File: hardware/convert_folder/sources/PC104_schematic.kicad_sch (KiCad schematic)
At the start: 33 parts, among them CN20 PC104_inverted, CN21 PC104, CN22 PC104, CN23 PC104, CN24 PC104, CN25 PC104

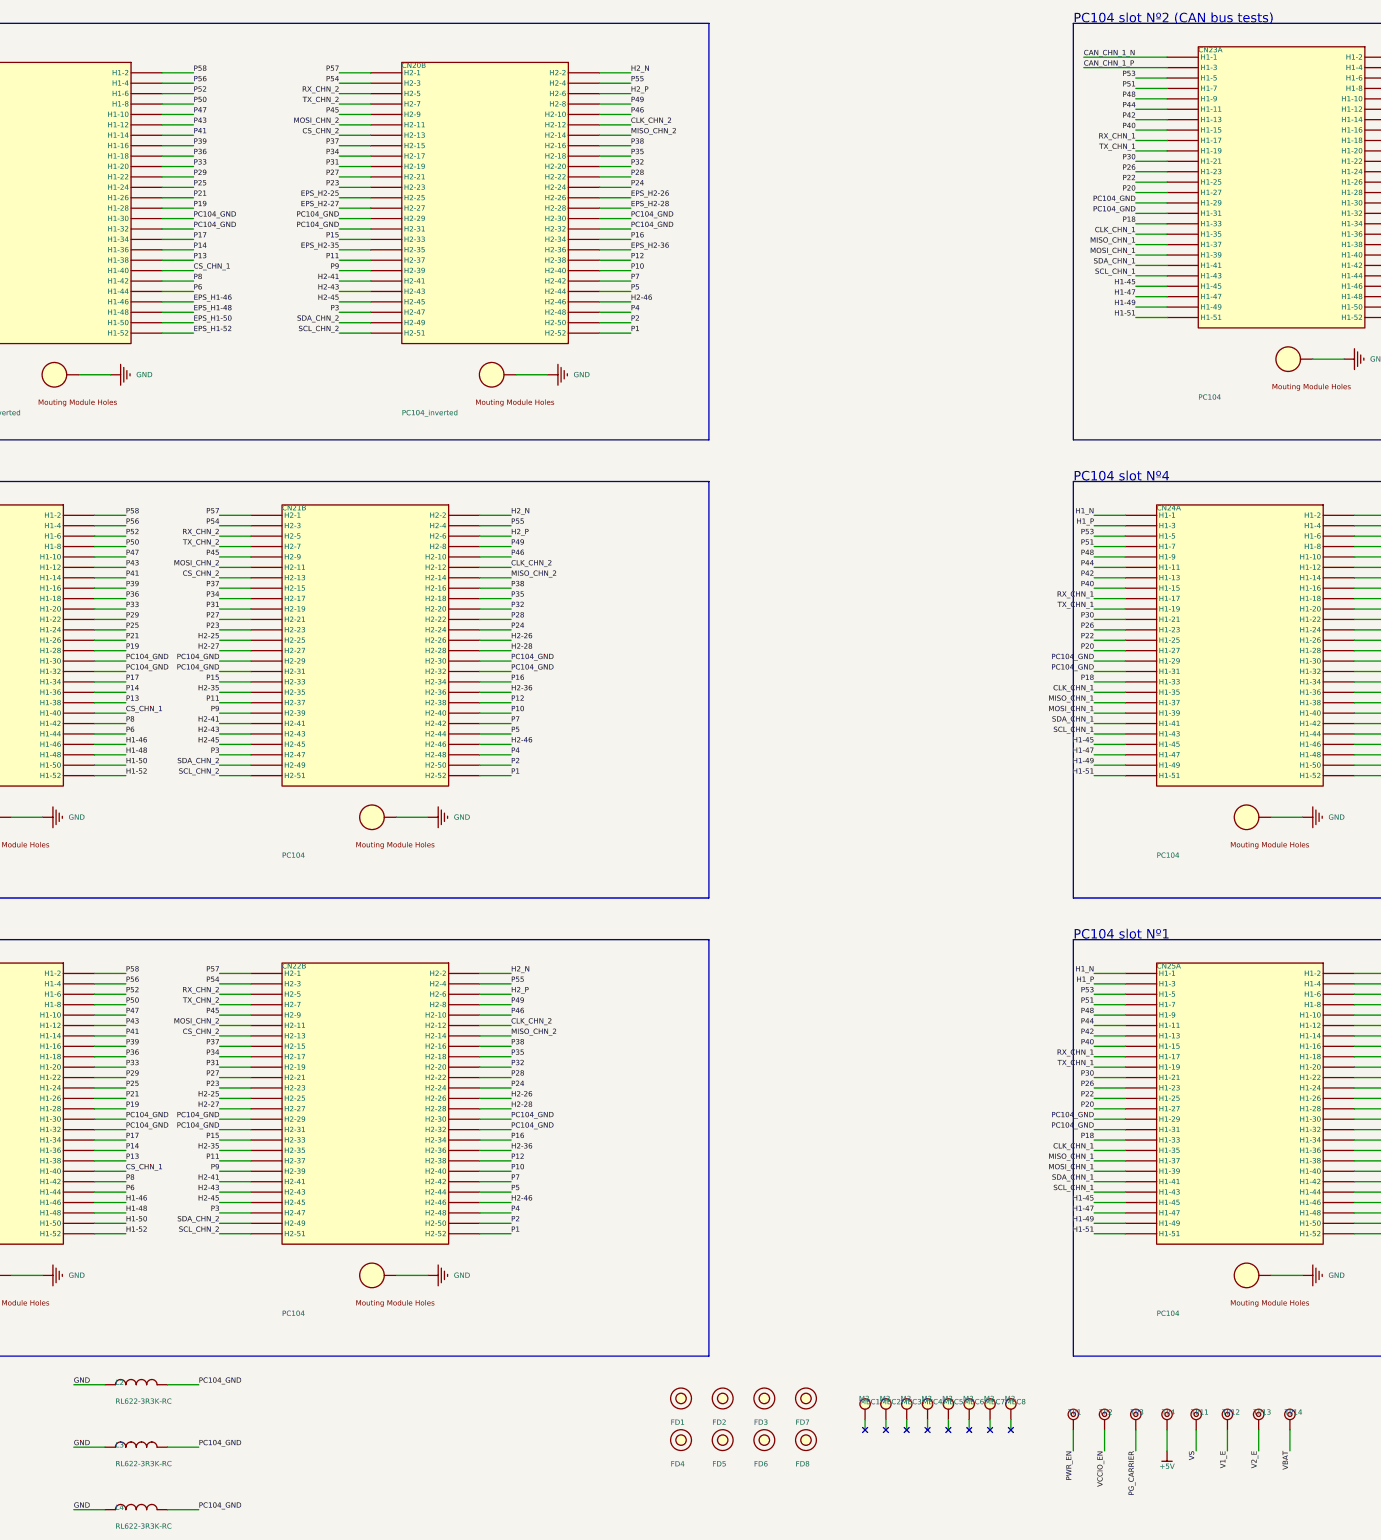
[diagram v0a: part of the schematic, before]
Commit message: fix: fix a lot of connections between blocks. Many more to go...
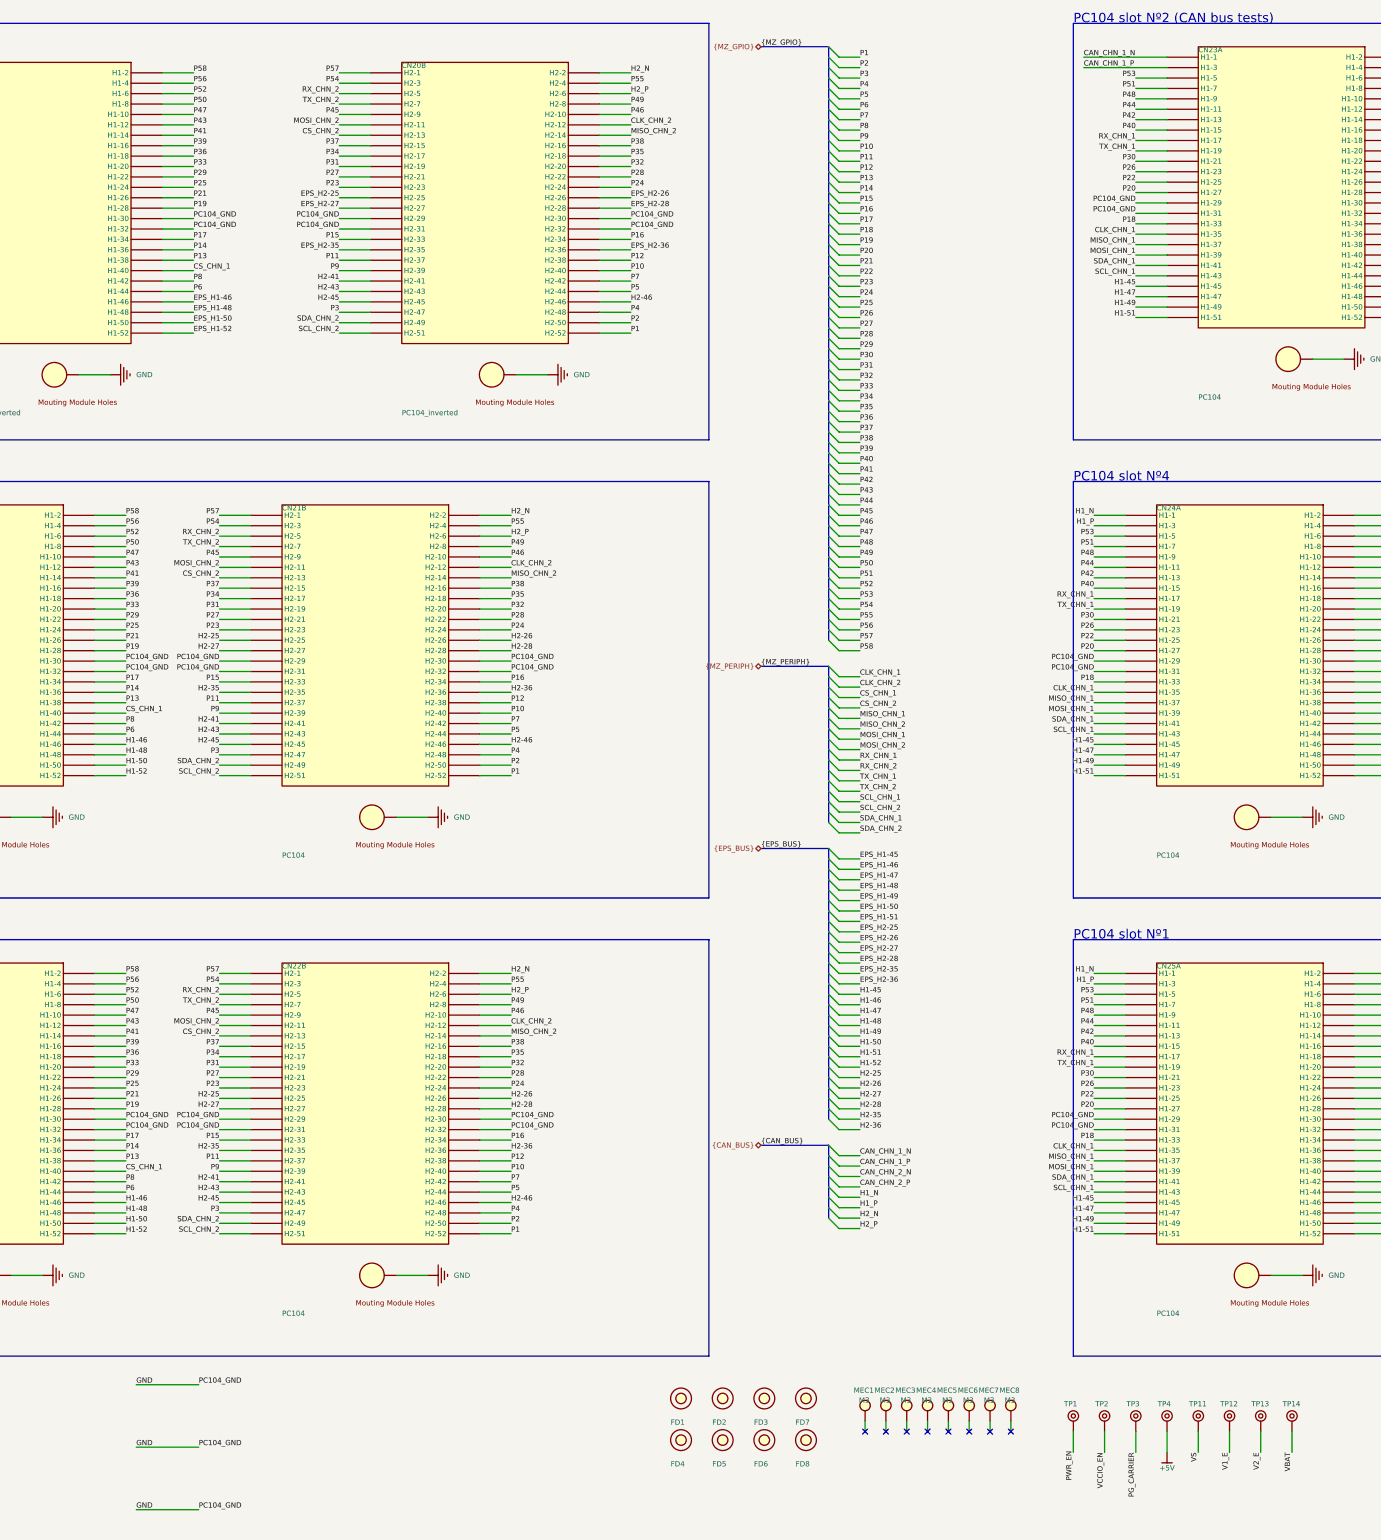
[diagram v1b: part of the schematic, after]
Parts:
- removed L2, L3, L4: RL622-3R3K-RC, RL622, symbol flatsat_platform_2:root_0_RL622-3R3K-RC_flatsat_platform_2.SchLib
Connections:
- net PC104_GND is gone; now on net GND: CN20.29 (H1-29), CN20.30 (H1-30), CN20.31 (H1-31), CN20.32 (H1-32), CN20.81 (H2-29), CN20.82 (H2-30), CN20.83 (H2-31), CN20.84 (H2-32), CN21.29 (H1-29), CN21.30 (H1-30), CN21.31 (H1-31), CN21.32 (H1-32), CN21.81 (H2-29), CN21.82 (H2-30), CN21.83 (H2-31), CN21.84 (H2-32), CN22.29 (H1-29), CN22.30 (H1-30), CN22.31 (H1-31), CN22.32 (H1-32), CN22.81 (H2-29), CN22.82 (H2-30), CN22.83 (H2-31), CN22.84 (H2-32), CN23.29 (H1-29), CN23.30 (H1-30), CN23.31 (H1-31), CN23.32 (H1-32), CN23.81 (H2-29), CN23.82 (H2-30), CN23.83 (H2-31), CN23.84 (H2-32), CN24.29 (H1-29), CN24.30 (H1-30), CN24.31 (H1-31), CN24.32 (H1-32), CN24.81 (H2-29), CN24.82 (H2-30), CN24.83 (H2-31), CN24.84 (H2-32), CN25.29 (H1-29), CN25.30 (H1-30), CN25.31 (H1-31), CN25.32 (H1-32), CN25.81 (H2-29), CN25.82 (H2-30), CN25.83 (H2-31), CN25.84 (H2-32)
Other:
- moved on the sheet: TP11, TP12, TP13, TP14

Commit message: fix: convert 90% of the schematic (there are 21 warnings/errors to resolve)
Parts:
- removed TP1, TP11, TP12, TP13, TP14, TP2, TP3, TP4: ~, TEST POINT PTH, symbol flatsat_platform_2:root_0_Test Point PTH_flatsat_platform_2.SchLib
- CN20: footprint PC104_inverted -> altium_import:PC104_INVERTED; symbol flatsat_platform_2:root_0_PC104_inverted_flatsat_platform_2.SchLib -> altium_import:root_0_PC104_inverted_flatsat_platform_2.SchLib; MANUFACTURER PART NUMBER TSW-126-07-G-D -> (none)
- CN21, CN22, CN23, CN24, CN25: footprint PC104 -> altium_import:PC104; symbol flatsat_platform_2:root_0_PC104_flatsat_platform_2.SchLib -> altium_import:root_0_PC104_flatsat_platform_2.SchLib; MANUFACTURER PART NUMBER SSW-126-01-G-D -> (none)
- FD1, FD2, FD3, FD4, FD5, FD6, FD7, FD8: footprint Fiducial 1.3mm -> altium_import:Fiducial 1.3mm; symbol flatsat_platform_2:root_0_Fiducial 1.3_flatsat_platform_2.SchLib -> altium_import:root_0_Fiducial 1.3_flatsat_platform_2.SchLib
- MEC1, MEC2, MEC3, MEC4, MEC5, MEC6, MEC7, MEC8: footprint M3 hole -> altium_import:M3 HOLE; symbol flatsat_platform_2:root_0_M3 hole_flatsat_platform_2.SchLib -> altium_import:root_0_M3 hole_flatsat_platform_2.SchLib
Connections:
- net GND: no longer CN20.0 (Mouting), CN21.0 (Mouting), CN22.0 (Mouting), CN23.0 (Mouting), CN24.0 (Mouting), CN25.0 (Mouting)
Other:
- moved on the sheet: CN20A, CN21A, CN22A, CN23A, CN24A, CN25A

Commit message: fix: start the layout of power path
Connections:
- net EPS_H1-46 is gone; now on net EPS_H1-45: CN20.46 (H1-46)
- net EPS_H1-48 is gone; now on net EPS_H1-47: CN20.48 (H1-48)
- net EPS_H1-50 is gone; now on net EPS_H1-49: CN20.50 (H1-50)
- net EPS_H1-52 is gone; now on net EPS_H1-51: CN20.52 (H1-52)
- net EPS_H2-26 is gone; now on net EPS_H2-25: CN20.78 (H2-26)
- net EPS_H2-28 is gone; now on net EPS_H2-27: CN20.80 (H2-28)
- net EPS_H2-36 is gone; now on net EPS_H2-35: CN20.88 (H2-36)
- net H1-46 is gone; now on net H1-45: CN21.46 (H1-46), CN22.46 (H1-46), CN23.46 (H1-46), CN24.46 (H1-46), CN25.46 (H1-46)
- net H1-48 is gone; now on net H1-47: CN21.48 (H1-48), CN22.48 (H1-48), CN23.48 (H1-48), CN24.48 (H1-48), CN25.48 (H1-48)
- net H1-50 is gone; now on net H1-49: CN21.50 (H1-50), CN22.50 (H1-50), CN23.50 (H1-50), CN24.50 (H1-50), CN25.50 (H1-50)
- net H1-52 is gone; now on net H1-51: CN21.52 (H1-52), CN22.52 (H1-52), CN23.52 (H1-52), CN24.52 (H1-52), CN25.52 (H1-52)
- net H2-26 is gone; now on net H2-25: CN21.78 (H2-26), CN22.78 (H2-26), CN23.78 (H2-26), CN24.78 (H2-26), CN25.78 (H2-26)
- net H2-28 is gone; now on net H2-27: CN21.80 (H2-28), CN22.80 (H2-28), CN23.80 (H2-28), CN24.80 (H2-28), CN25.80 (H2-28)
- net H2-36 is gone; now on net H2-35: CN21.88 (H2-36), CN22.88 (H2-36), CN23.88 (H2-36), CN24.88 (H2-36), CN25.88 (H2-36)

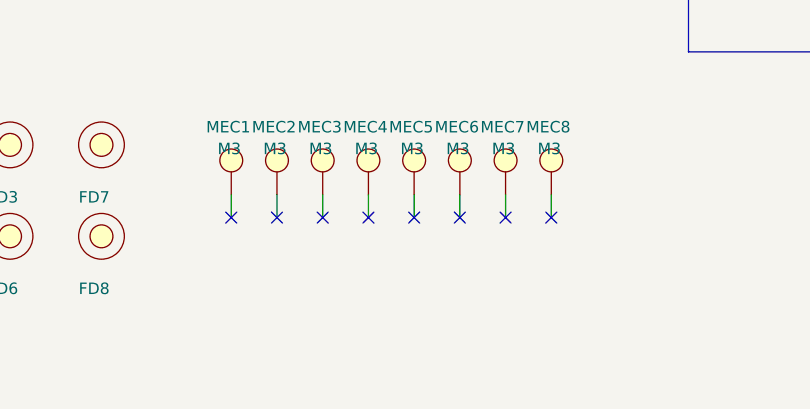
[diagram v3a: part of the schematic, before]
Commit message: fix: fix the position of communication protocol signals on the MicroZed
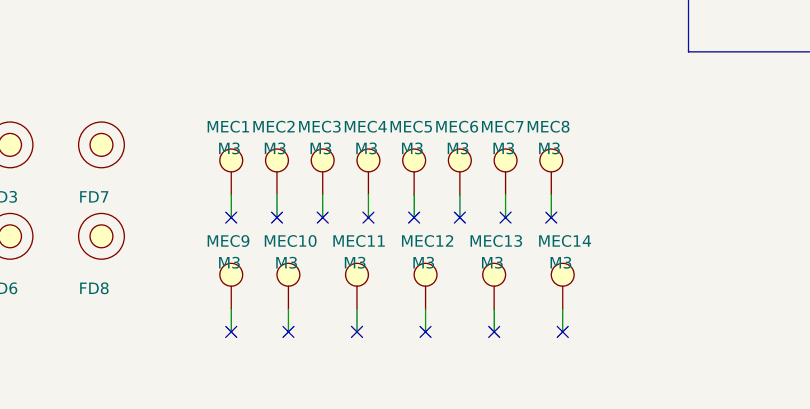
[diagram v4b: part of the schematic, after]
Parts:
- added MEC10, MEC11, MEC12, MEC13, MEC14, MEC9: M3, altium_import:M3 HOLE, symbol altium_import:root_0_M3 hole_flatsat_platform_2.SchLib
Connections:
- no-connect marks 8 -> 14

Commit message: fix: minor corrections at the TPS3780 circuit
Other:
- moved on the sheet: CN21A, CN21B, CN22A, CN22B, CN24A, CN24B, CN25A, CN25B

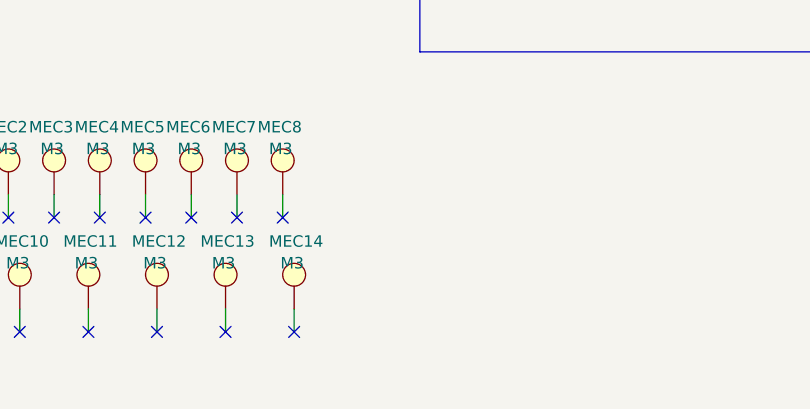
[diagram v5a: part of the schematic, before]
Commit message: fix: fix caps. values, add decoupling capacitors for INAs and other ICs, and add general improvements
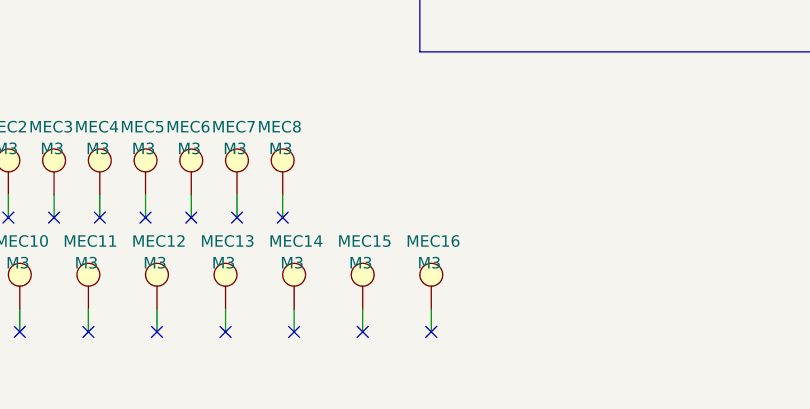
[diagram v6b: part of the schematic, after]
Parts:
- added MEC15, MEC16: M3, altium_import:M3 HOLE, symbol altium_import:root_0_M3 hole_flatsat_platform_2.SchLib
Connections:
- no-connect marks 14 -> 16
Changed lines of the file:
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@@
 	)
 	(no_connect
+		(at 331.47 394.97)
+	)
+	(no_connect
 		(at 289.56 382.27)
 	)
@@
 		(at 299.72 382.27)
 	)
+	(no_connect
+		(at 323.85 394.97)
+	)
 	(bus_entry
 		(at 270.51 92.71)
@@
 	(wire
 		(pts
+			(xy 331.47 392.43) (xy 331.47 394.97)
+		)
+		(stroke
+			(width 0)
+			(type default)
+		)
+	)
+	(wire
+		(pts
 			(xy 52.07 193.04) (xy 44.45 193.04)
 		)
@@
 		)
 	)
+	(wire
+		(pts
+			(xy 323.85 392.43) (xy 323.85 394.97)
+		)
+		(stroke
+			(width 0)
+			(type default)
+		)
+	)
 	(bus
 		(pts
@@
 					(unit 1)
 				)
+			)
+		)
+	)
+	(symbol
+		(lib_id "altium_import:root_0_M3 hole_flatsat_platform_2.SchLib")
+		(at 331.47 388.62 90)
+		(unit 1)
+		(exclude_from_sim no)
+		(in_bom yes)
+		(on_board yes)
+		(dnp no)
+		(property "Reference" "MEC16"
+			(at 328.676 384.175 90)
+			(effects
+				(font
+					(size 1.27 1.27)
+				)
+				(justify right bottom)
+			)
+		)
+		(property "Value" "M3"
+			(at 329.946 386.588 90)
+			(effects
+				(font
+					(size 1.27 1.27)
+				)
+				(justify right bottom)
+			)
+		)
+		(property "Footprint" "altium_import:M3 HOLE"
+			(at 331.47 388.62 0)
+			(effects
+				(font
+					(size 1.27 1.27)
+				)
+				(hide yes)
+			)
+		)
+		(property "Datasheet" ""
+			(at 331.47 388.62 0)
+			(effects
+				(font
+					(size 1.27 1.27)
+				)
+				(hide yes)
+			)
+		)
+		(property "Description" "M3 hole"
+			(at 331.47 388.62 0)
+			(effects
+				(font
+					(size 1.27 1.27)
+				)
+				(hide yes)
+			)
+		)
+		(pin "0"
+		)
+		(instances
+			(project "flatsat_platform_2"
+				(path "/8c88a7e1-4137-48d7-b926-b5e762e3852f/a83a7b28-9eff-4d1f-80e0-c5fbfa98ea5b"
+					(reference "MEC16")
+					(unit 1)
+				)
+			)
+		)
+	)
+	(symbol
+		(lib_id "altium_import:root_0_M3 hole_flatsat_platform_2.SchLib")
+		(at 323.85 388.62 90)
+		(unit 1)
+		(exclude_from_sim no)
+		(in_bom yes)
+		(on_board yes)
+		(dnp no)
+		(property "Reference" "MEC15"
+			(at 321.056 384.175 90)
+			(effects
+				(font
+					(size 1.27 1.27)
+				)
+				(justify right bottom)
+			)
+		)
+		(property "Value" "M3"
+			(at 322.326 386.588 90)
+			(effects
+				(font
+					(size 1.27 1.27)
+				)
+				(justify right bottom)
+			)
+		)
+		(property "Footprint" "altium_import:M3 HOLE"
+			(at 323.85 388.62 0)
+			(effects
+				(font
+					(size 1.27 1.27)
+				)
+				(hide yes)
+			)
+		)
+		(property "Datasheet" ""
+			(at 323.85 388.62 0)
+			(effects
+				(font
+					(size 1.27 1.27)
+				)
+				(hide yes)
+			)
+		)
+		(property "Description" "M3 hole"
+			(at 323.85 388.62 0)
+			(effects
+				(font
+					(size 1.27 1.27)
+				)
+				(hide yes)
+			)
+		)
+		(pin "0"
+		)
+		(instances
+			(project "flatsat_platform_2"
+				(path "/8c88a7e1-4137-48d7-b926-b5e762e3852f/a83a7b28-9eff-4d1f-80e0-c5fbfa98ea5b"
+					(reference "MEC15")
+					(unit 1)
+				)
